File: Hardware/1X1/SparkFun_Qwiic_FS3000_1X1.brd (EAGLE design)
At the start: 25.4 x 25.4 mm, 58 parts, among them J2 QWIIC_RA, J3 QWIIC_RA, U1 FS3000

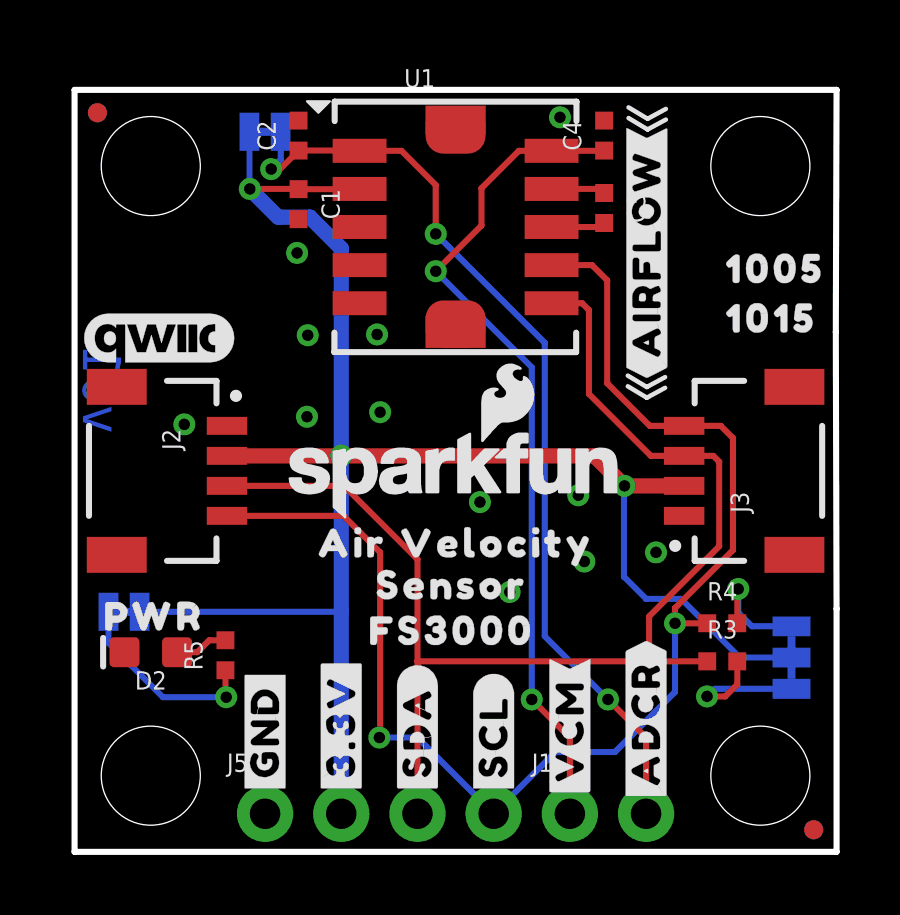
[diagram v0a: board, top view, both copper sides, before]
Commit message: eng ran checklist before double-check request
-dimensions were off grid slightly, corrected [1X1 version].
-approved DRC overlap error on jumper [1X1 version].
-added a couple more stitching GND vias [1X1]
-updated pad 3 to extend longer as shown in datasheet [both versions]
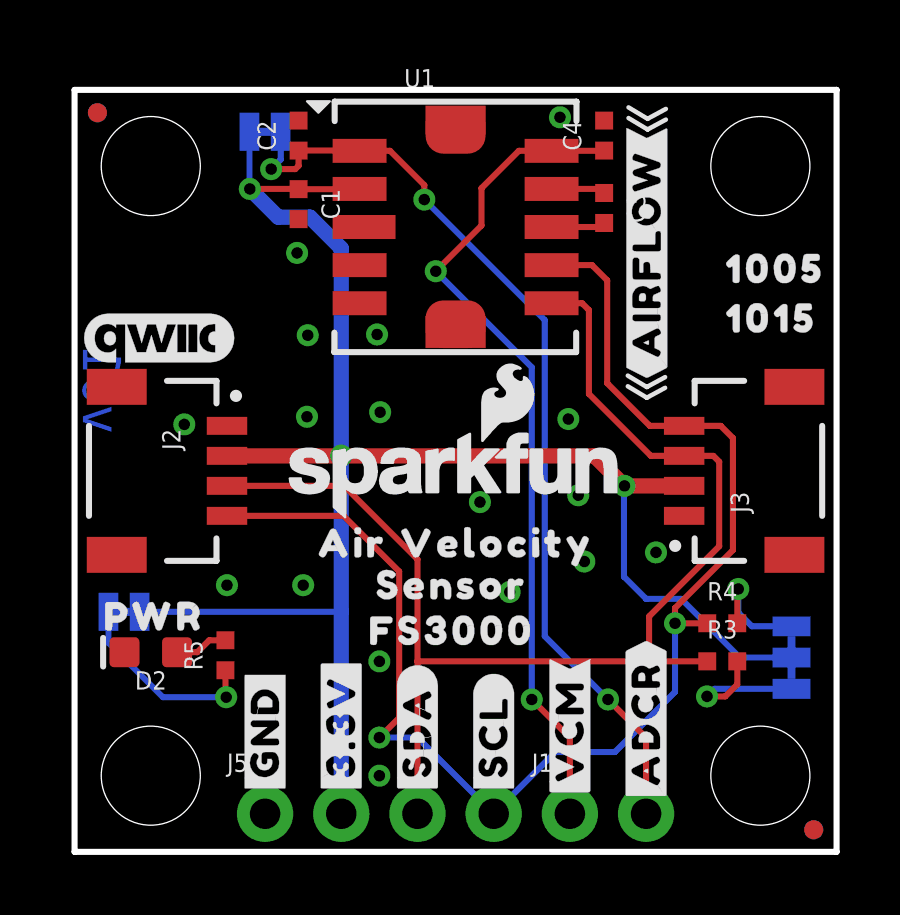
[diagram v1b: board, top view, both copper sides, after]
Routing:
- net SCL: track 45.2 -> 45.7 mm
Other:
- outline, holes or cut-outs redrawn
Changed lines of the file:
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@@
 <layer number="27" name="tValues" color="7" fill="1" visible="no" active="yes"/>
 <layer number="28" name="bValues" color="7" fill="1" visible="no" active="yes"/>
-<layer number="29" name="tStop" color="7" fill="3" visible="no" active="yes"/>
+<layer number="29" name="tStop" color="7" fill="3" visible="yes" active="yes"/>
 <layer number="30" name="bStop" color="7" fill="6" visible="no" active="yes"/>
 <layer number="31" name="tCream" color="7" fill="4" visible="no" active="yes"/>
@@
 <layer number="45" name="Holes" color="7" fill="1" visible="yes" active="yes"/>
 <layer number="46" name="Milling" color="3" fill="1" visible="no" active="yes"/>
-<layer number="47" name="Measures" color="7" fill="1" visible="no" active="yes"/>
+<layer number="47" name="Measures" color="7" fill="1" visible="yes" active="yes"/>
 <layer number="48" name="Document" color="7" fill="1" visible="no" active="yes"/>
-<layer number="49" name="Reference" color="7" fill="1" visible="no" active="yes"/>
+<layer number="49" name="Reference" color="7" fill="1" visible="yes" active="yes"/>
 <layer number="50" name="dxf" color="7" fill="1" visible="no" active="yes"/>
 <layer number="51" name="tDocu" color="6" fill="1" visible="yes" active="yes"/>
@@
 <wire x1="0" y1="0" x2="0" y2="25.4" width="0.2032" layer="20"/>
 <wire x1="0" y1="25.4" x2="25.4" y2="25.4" width="0.2032" layer="20"/>
-<wire x1="25.4" y1="25.4" x2="25.3746" y2="17.3228" width="0.2032" layer="20"/>
-<wire x1="25.3746" y1="17.3228" x2="25.4" y2="8.1026" width="0.2032" layer="20"/>
-<wire x1="25.4" y1="8.1026" x2="25.4" y2="0" width="0.2032" layer="20"/>
+<wire x1="25.4" y1="25.4" x2="25.4" y2="0" width="0.2032" layer="20"/>
 <wire x1="25.4" y1="0" x2="0" y2="0" width="0.2032" layer="20"/>
 <text x="0.9144" y="15.4178" size="1.27" layer="16" font="vector" ratio="15" rot="SMR90" align="center">v01</text>
 <dimension x1="0" y1="25.4" x2="0" y2="0" x3="-12.7" y3="12.7" textsize="1.27" layer="47" unit="inch"/>
 <text x="13.97" y="-12.7" size="1.778" layer="51" font="vector">Pete Lewis</text>
-<dimension x1="0" y1="25.4" x2="25.4" y2="25.4" x3="12.7" y3="39.37" textsize="1.27" layer="47" unit="inch"/>
+<dimension x1="0" y1="25.4" x2="25.4" y2="25.4" x3="12.7" y3="35.56" textsize="1.27" layer="47" unit="inch"/>
 <dimension x1="2.54" y1="2.54" x2="2.54" y2="22.86" x3="-8.89" y3="12.7" textsize="1.27" layer="47" unit="inch"/>
 <dimension x1="0" y1="0" x2="0" y2="2.54" x3="-1.27" y3="1.27" textsize="1.27" layer="47" unit="inch"/>
@@
 <dimension x1="0" y1="25.4" x2="0" y2="22.86" x3="-6.35" y3="24.13" textsize="1.27" layer="47" unit="inch"/>
 <text x="-3.81" y="-16.51" size="1.778" layer="47" font="vector">Measure Units: INCHES</text>
-<dimension x1="0" y1="25.4" x2="15.24" y2="25.4" x3="7.62" y3="35.56" textsize="1.27" layer="47" unit="inch"/>
-<dimension x1="15.2146" y1="17.3228" x2="25.3746" y2="17.3228" x3="20.2946" y3="35.56" textsize="1.27" layer="47" unit="inch"/>
-<dimension x1="25.3746" y1="17.3228" x2="25.4" y2="8.1026" x3="30.479928125" y3="12.726728125" textsize="1.27" layer="47" unit="inch"/>
 <dimension x1="0" y1="0" x2="6.35" y2="1.27" x3="3.175" y3="-2.8702" textsize="1.27" layer="47" dtype="horizontal" unit="inch"/>
 <dimension x1="0" y1="0" x2="5.08" y2="12.7" x3="-5.2324" y3="6.35" textsize="1.27" layer="47" dtype="vertical" unit="inch"/>
-<dimension x1="0" y1="25.4" x2="11.43" y2="24.13" x3="5.715" y3="31.75" textsize="1.27" layer="47" dtype="horizontal" unit="inch"/>
-<dimension x1="25.3746" y1="17.3228" x2="19.685" y2="12.7" x3="22.5298" y3="21.59" textsize="1.27" layer="47" dtype="horizontal" unit="inch"/>
 <wire x1="19.7104" y1="24.4094" x2="19.1008" y2="24.0792" width="0.1524" layer="21"/>
 <wire x1="19.1008" y1="24.0792" x2="18.4658" y2="24.4602" width="0.1524" layer="21"/>
@@
 <rectangle x1="20.5105" y1="17.272" x2="20.955" y2="18.3515" layer="29"/>
 <rectangle x1="21.1455" y1="17.272" x2="21.59" y2="18.3515" layer="29"/>
+<dimension x1="0" y1="25.4" x2="12.7" y2="21.59" x3="6.35" y3="31.75" textsize="1.27" textratio="15" layer="47" dtype="horizontal" unit="inch"/>
+<dimension x1="25.4" y1="25.4" x2="22.86" y2="22.86" x3="24.13" y3="27.94" textsize="1.27" textratio="15" layer="47" dtype="horizontal" unit="inch"/>
+<dimension x1="25.4" y1="0" x2="22.86" y2="2.54" x3="29.21" y3="1.27" textsize="1.27" textratio="15" layer="47" dtype="vertical" unit="inch"/>
+<dimension x1="22.86" y1="22.86" x2="22.86" y2="25.4" x3="34.29" y3="24.13" textsize="1.27" textratio="15" layer="47" dtype="vertical" unit="inch"/>
 </plain>
 <attributes>
@@
 <via x="14.5034" y="8.6614" extent="1-16" drill="0.381"/>
 <via x="13.5128" y="11.6586" extent="1-16" drill="0.381"/>
+<via x="7.62" y="8.89" extent="1-16" drill="0.381"/>
+<via x="5.08" y="8.89" extent="1-16" drill="0.381"/>
+<via x="10.16" y="2.54" extent="1-16" drill="0.381"/>
+<via x="10.16" y="6.35" extent="1-16" drill="0.381"/>
+<via x="16.4592" y="14.4272" extent="1-16" drill="0.381"/>
 </signal>
 <signal name="SCL">
@@
 <wire x1="19.1756" y1="14.2" x2="20.32" y2="14.2" width="0.2032" layer="1"/>
 <wire x1="5.08" y1="11.2" x2="8.9676" y2="11.2" width="0.2032" layer="1"/>
-<wire x1="8.9676" y1="11.2" x2="10.1854" y2="9.9822" width="0.2032" layer="1"/>
-<wire x1="10.1854" y1="9.9822" x2="10.1854" y2="3.8354" width="0.2032" layer="1"/>
-<wire x1="10.1854" y1="3.8354" x2="10.16" y2="3.81" width="0.2032" layer="1"/>
+<wire x1="8.9676" y1="11.2" x2="10.8204" y2="9.3472" width="0.2032" layer="1"/>
+<wire x1="10.8204" y1="9.3472" x2="10.8204" y2="4.4704" width="0.2032" layer="1"/>
+<wire x1="10.8204" y1="4.4704" x2="10.16" y2="3.81" width="0.2032" layer="1"/>
 <via x="10.16" y="3.81" extent="1-16" drill="0.381"/>
 <wire x1="10.16" y1="3.81" x2="11.43" y2="3.81" width="0.2032" layer="16"/>
@@
 <wire x1="9.5" y1="23.368" x2="9.492" y2="23.376" width="0.2032" layer="1"/>
 <wire x1="9.492" y1="23.376" x2="7.4676" y2="23.376" width="0.2032" layer="1"/>
-<wire x1="7.4676" y1="23.376" x2="6.85" y2="22.7584" width="0.2032" layer="1"/>
-<wire x1="6.85" y1="22.7584" x2="6.5532" y2="22.7584" width="0.2032" layer="1"/>
+<wire x1="7.4676" y1="23.376" x2="7.4676" y2="22.868" width="0.2032" layer="1"/>
+<wire x1="7.4676" y1="22.868" x2="7.358" y2="22.7584" width="0.2032" layer="1"/>
+<wire x1="7.358" y1="22.7584" x2="6.5532" y2="22.7584" width="0.2032" layer="1"/>
 <via x="6.5532" y="22.7584" extent="1-16" drill="0.381"/>
 <wire x1="6.5532" y1="22.7584" x2="6.8707" y2="23.0759" width="0.2032" layer="16"/>
 <wire x1="6.8707" y1="23.0759" x2="6.8707" y2="24.003" width="0.2032" layer="16"/>
-<wire x1="9.5" y1="23.368" x2="10.8966" y2="23.368" width="0.2032" layer="1"/>
-<wire x1="12.0396" y1="22.225" x2="12.0396" y2="20.5994" width="0.2032" layer="1"/>
-<via x="12.0396" y="20.5994" extent="1-16" drill="0.381"/>
-<wire x1="12.0396" y1="20.5994" x2="15.6718" y2="16.9672" width="0.2032" layer="16"/>
-<wire x1="10.8966" y1="23.368" x2="12.0396" y2="22.225" width="0.2032" layer="1"/>
+<wire x1="9.5" y1="23.368" x2="10.5156" y2="23.368" width="0.2032" layer="1"/>
+<wire x1="11.6586" y1="22.225" x2="11.6586" y2="21.7424" width="0.2032" layer="1"/>
+<via x="11.6586" y="21.7424" extent="1-16" drill="0.381"/>
+<wire x1="11.6586" y1="21.7424" x2="15.6718" y2="17.7292" width="0.2032" layer="16"/>
+<wire x1="10.5156" y1="23.368" x2="11.6586" y2="22.225" width="0.2032" layer="1"/>
 <wire x1="19.05" y1="1.27" x2="19.05" y2="3.81" width="0.2032" layer="1"/>
 <wire x1="19.05" y1="3.81" x2="17.78" y2="5.08" width="0.2032" layer="1"/>
 <via x="17.78" y="5.08" extent="1-16" drill="0.381"/>
 <wire x1="17.78" y1="5.08" x2="15.6718" y2="7.1882" width="0.2032" layer="16"/>
-<wire x1="15.6718" y1="7.1882" x2="15.6718" y2="16.9672" width="0.2032" layer="16"/>
+<wire x1="15.6718" y1="7.1882" x2="15.6718" y2="17.7292" width="0.2032" layer="16"/>
 </signal>
 </signals>

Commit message: updated some stuff to correct recent libraries
-GNDs, Fiducials, and standoffs were still in old library. updated.
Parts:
- JP11, JP2, JP5, JP6: device SparkFun:MICRO-FIDUCIAL -> SparkFun-Aesthetics:FIDUCIAL-MICRO
- JP3, JP4, JP7, JP8: device SparkFun:STAND-OFF -> SparkFun-Hardware:STAND-OFF
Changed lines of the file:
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@@
 <layer number="27" name="tValues" color="7" fill="1" visible="no" active="yes"/>
 <layer number="28" name="bValues" color="7" fill="1" visible="no" active="yes"/>
-<layer number="29" name="tStop" color="7" fill="3" visible="yes" active="yes"/>
+<layer number="29" name="tStop" color="7" fill="3" visible="no" active="yes"/>
 <layer number="30" name="bStop" color="7" fill="6" visible="no" active="yes"/>
 <layer number="31" name="tCream" color="7" fill="4" visible="no" active="yes"/>
@@
 <layer number="45" name="Holes" color="7" fill="1" visible="yes" active="yes"/>
 <layer number="46" name="Milling" color="3" fill="1" visible="no" active="yes"/>
-<layer number="47" name="Measures" color="7" fill="1" visible="yes" active="yes"/>
+<layer number="47" name="Measures" color="7" fill="1" visible="no" active="yes"/>
 <layer number="48" name="Document" color="7" fill="1" visible="no" active="yes"/>
-<layer number="49" name="Reference" color="7" fill="1" visible="yes" active="yes"/>
+<layer number="49" name="Reference" color="7" fill="1" visible="no" active="yes"/>
 <layer number="50" name="dxf" color="7" fill="1" visible="no" active="yes"/>
 <layer number="51" name="tDocu" color="6" fill="1" visible="yes" active="yes"/>
@@
 </autorouter>
 <elements>
-<element name="JP3" library="SparkFun" package="STAND-OFF" value="STAND-OFF" x="2.54" y="22.86" smashed="yes"/>
-<element name="JP2" library="SparkFun" package="MICRO-FIDUCIAL" value="FIDUCIALUFIDUCIAL" x="24.638" y="0.7366" smashed="yes"/>
-<element name="JP6" library="SparkFun" package="MICRO-FIDUCIAL" value="FIDUCIALUFIDUCIAL" x="0.762" y="24.638" smashed="yes"/>
+<element name="JP3" library="SparkFun-Hardware" package="STAND-OFF" value="STAND-OFF" x="2.54" y="22.86" smashed="yes"/>
+<element name="JP2" library="SparkFun-Aesthetics" package="FIDUCIAL-MICRO" value="FIDUCIALUFIDUCIAL" x="24.638" y="0.7366" smashed="yes"/>
+<element name="JP6" library="SparkFun-Aesthetics" package="FIDUCIAL-MICRO" value="FIDUCIALUFIDUCIAL" x="0.762" y="24.638" smashed="yes"/>
 <element name="R4" library="SparkFun-Resistors" package="0402-TIGHT" value="2.2k" x="21.59" y="7.62" smashed="yes">
 <attribute name="NAME" x="21.59" y="8.382" size="0.6096" layer="25" font="vector" ratio="20" align="bottom-center"/>
@@
 </element>
 <element name="LOGO1" library="SparkFun-Aesthetics" package="OSHW-LOGO-MINI" value="OSHW-LOGOMINI" x="2.5146" y="19.177" smashed="yes" rot="MR0"/>
-<element name="JP11" library="SparkFun" package="MICRO-FIDUCIAL" value="FIDUCIALUFIDUCIAL" x="24.638" y="0.7366" smashed="yes" rot="MR0"/>
-<element name="JP5" library="SparkFun" package="MICRO-FIDUCIAL" value="FIDUCIALUFIDUCIAL" x="0.762" y="24.638" smashed="yes" rot="MR0"/>
+<element name="JP11" library="SparkFun-Aesthetics" package="FIDUCIAL-MICRO" value="FIDUCIALUFIDUCIAL" x="24.638" y="0.7366" smashed="yes" rot="MR0"/>
+<element name="JP5" library="SparkFun-Aesthetics" package="FIDUCIAL-MICRO" value="FIDUCIALUFIDUCIAL" x="0.762" y="24.638" smashed="yes" rot="MR0"/>
 <element name="J5" library="SparkFun-Connectors" package="1X04_NO_SILK" value="" x="6.35" y="1.27" smashed="yes">
 <attribute name="NAME" x="5.08" y="2.667" size="0.6096" layer="25" font="vector" ratio="20"/>
@@
 </element>
 <element name="LOGO4" library="SparkFun-Aesthetics" package="QWIIC_5MM" value="QWIIC_LOGO_5MM" x="2.794" y="17.145" smashed="yes"/>
-<element name="JP8" library="SparkFun" package="STAND-OFF" value="STAND-OFF" x="2.54" y="2.54" smashed="yes"/>
+<element name="JP8" library="SparkFun-Hardware" package="STAND-OFF" value="STAND-OFF" x="2.54" y="2.54" smashed="yes"/>
 <element name="U$5" library="output" package="#GND#0" value="" x="6.35" y="1.778" smashed="yes" rot="R90"/>
 <element name="U$6" library="output" package="#GND#0" value="" x="6.35" y="1.778" smashed="yes" rot="MR90"/>
@@
 <element name="U$21" library="output" package="AIR30004" value="" x="18.7706" y="19.5326" smashed="yes" rot="MR0"/>
 <element name="U$22" library="output" package="SENSOR30005" value="" x="19.05" y="16.7894" smashed="yes" rot="MR0"/>
-<element name="JP4" library="SparkFun" package="STAND-OFF" value="STAND-OFF" x="22.86" y="22.86" smashed="yes"/>
-<element name="JP7" library="SparkFun" package="STAND-OFF" value="STAND-OFF" x="22.86" y="2.54" smashed="yes"/>
+<element name="JP4" library="SparkFun-Hardware" package="STAND-OFF" value="STAND-OFF" x="22.86" y="22.86" smashed="yes"/>
+<element name="JP7" library="SparkFun-Hardware" package="STAND-OFF" value="STAND-OFF" x="22.86" y="2.54" smashed="yes"/>
 <element name="J3" library="SparkFun-Connectors" package="JST04_1MM_RA" value="QWIIC_RA" x="20.32" y="12.7" smashed="yes" rot="R90">
 <attribute name="NAME" x="22.479" y="11.303" size="0.6096" layer="25" font="vector" ratio="20" rot="R90"/>
